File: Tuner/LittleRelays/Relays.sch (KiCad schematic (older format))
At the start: 86 parts, among them J1 Conn_01x03, J10 Conn_01x02, J11 Conn_01x02, J12 Conn_01x01, J13 Conn_01x01, J14 Conn_01x01, J15 Conn_01x01, J16 Conn_01x02, J17 Conn_02x10_Odd_Even, J18 Conn_01x02, J19 Conn_01x03, J2 Conn_01x03, J3 Conn_01x03, J4 Conn_01x03, J5 Conn_01x03, J6 Conn_01x03, J7 Conn_01x03, J8 Conn_01x02, J9 Conn_01x02

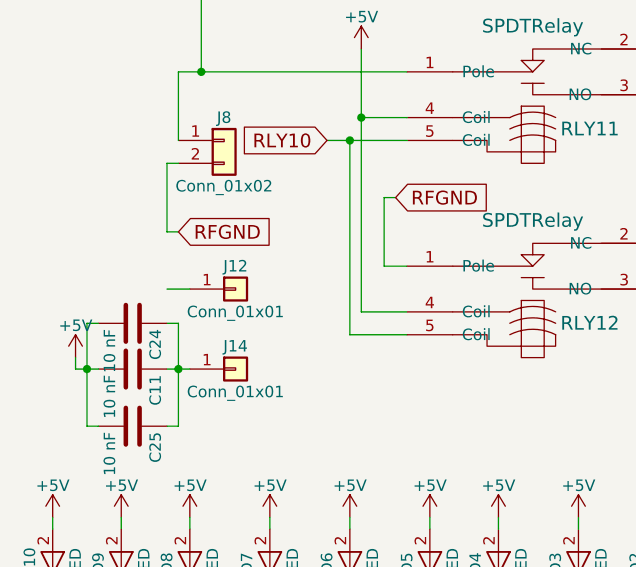
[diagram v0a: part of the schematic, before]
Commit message: Error in pinout HK19F fixed
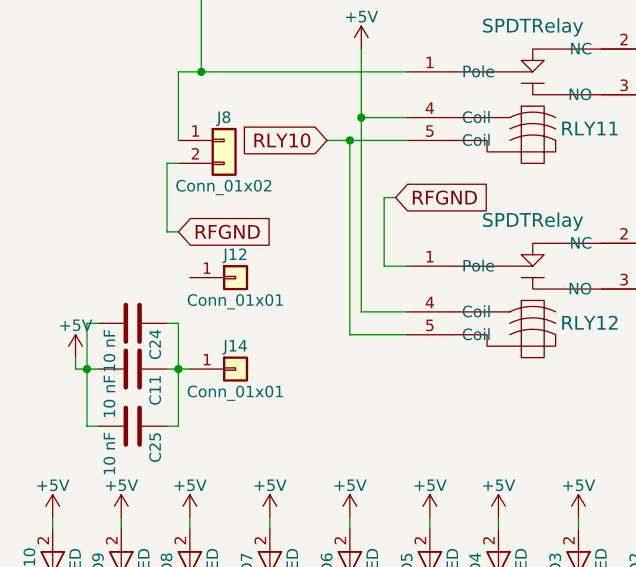
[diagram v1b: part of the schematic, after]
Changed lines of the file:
@@
 RLY10
-$Comp
-L Conn_01x01 J12
-U 1 1 5B1981D8
-P 1650 5400
-F 0 "J12" H 1650 5500 50  0000 C CNN
-F 1 "Conn_01x01" H 1650 5300 50  0000 C CNN
-F 2 "Connectors:1pin" H 1650 5400 50  0001 C CNN
-F 3 "" H 1650 5400 50  0001 C CNN
-	1    1650 5400
-	1    0    0    -1
-$EndComp
 $Comp
 L C C24
@@
 	7950 5400 8300 5400
 Wire Wire Line
-	1350 5400 1450 5400
-Wire Wire Line
 	1350 5550 1400 5550
 Wire Wire Line
 	1400 5550 1400 6000
 Connection ~ 1400 5750
-Wire Wire Line
-	1000 5550 1000 6000
 Wire Wire Line
 	1000 5550 1050 5550
@@
 	0    1    1    0
 $EndComp
+Wire Wire Line
+	1000 5550 1000 6000
+$Comp
+L Conn_01x01 J12
+U 1 1 5BCFCED9
+P 1650 5350
+F 0 "J12" H 1650 5450 50  0000 C CNN
+F 1 "Conn_01x01" H 1650 5250 50  0000 C CNN
+F 2 "Connectors:1pin" H 1650 5350 50  0001 C CNN
+F 3 "" H 1650 5350 50  0001 C CNN
+	1    1650 5350
+	1    0    0    -1
+$EndComp
 $EndSCHEMATC

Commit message: JLCPCB Nov 1 2018
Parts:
- removed C26: 10 nF, Capacitors_THT:C_Disc_D5.0mm_W2.5mm_P2.50mm, symbol C
- removed C27: 10 nF, Capacitors_THT:C_Disc_D5.0mm_W2.5mm_P5.00mm, symbol C
- added J20, J21, J22, J23, J24, J25, J26, J27, J28: Conn_01x01, tuner:SOLDERJUMPER, symbol Conn_01x01
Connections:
- net RFGND: now also J22.1 (Pin_1)
- net at J9.2 (Pin_2), RLY10.2 (NC): now also J23.1 (Pin_1)
- net at J10.2 (Pin_2), RLY10.3 (NO): now also J24.1 (Pin_1)
- net at J13.1 (Pin_1): now also J25.1 (Pin_1), J26.1 (Pin_1)
- net at J15.1 (Pin_1): now also J27.1 (Pin_1), J28.1 (Pin_1)
- net at J16.2 (Pin_2), RLY12.3 (NO): now also J21.1 (Pin_1)
- net at J11.2 (Pin_2), RLY12.2 (NC): now also J20.1 (Pin_1)
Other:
- moved on the sheet: J13, J15

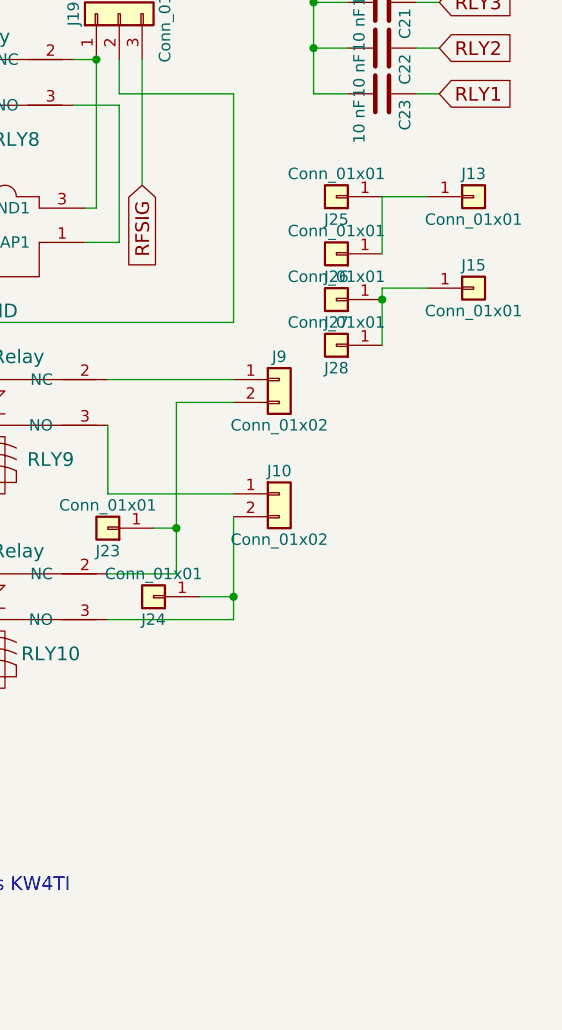
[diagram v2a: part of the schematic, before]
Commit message: Added extra capacitors between relay power and ground posts
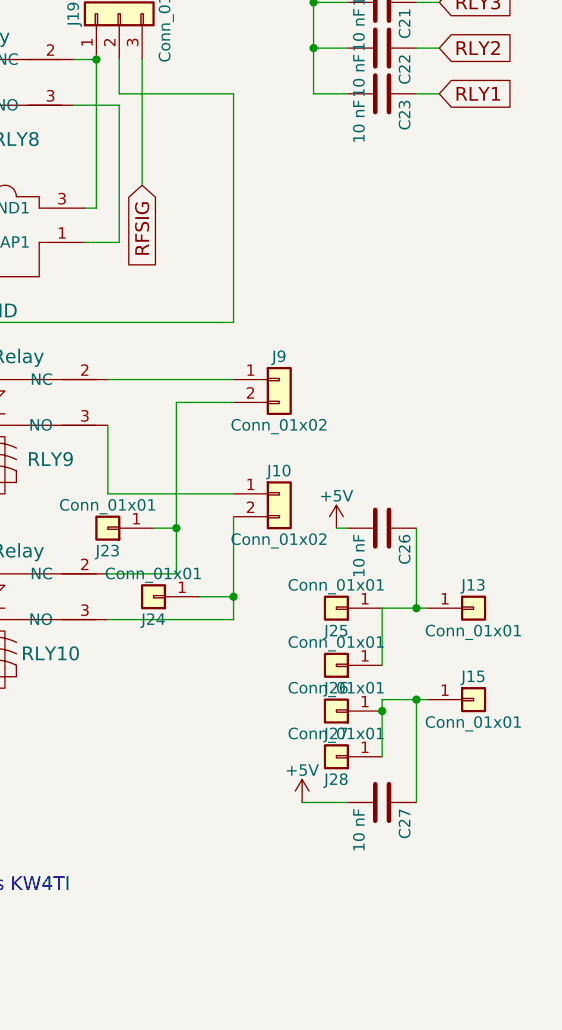
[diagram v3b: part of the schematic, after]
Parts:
- added C26, C27: 10 nF, Capacitors_THT:C_Disc_D5.0mm_W2.5mm_P2.50mm, symbol C
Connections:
- net +5V: now also C26.2, C27.2
- net at J13.1 (Pin_1), J25.1 (Pin_1), J26.1 (Pin_1): now also C26.1
- net at J15.1 (Pin_1), J27.1 (Pin_1), J28.1 (Pin_1): now also C27.1
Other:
- moved on the sheet: J13, J15, J25, J26, J27, J28
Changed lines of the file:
@@
 L Conn_01x01 J13
 U 1 1 5B19804D
-P 10950 3650
-F 0 "J13" H 10950 3750 50  0000 C CNN
-F 1 "Conn_01x01" H 10950 3550 50  0000 C CNN
-F 2 "Connectors:1pin" H 10950 3650 50  0001 C CNN
-F 3 "" H 10950 3650 50  0001 C CNN
-	1    10950 3650
+P 10950 5450
+F 0 "J13" H 10950 5550 50  0000 C CNN
+F 1 "Conn_01x01" H 10950 5350 50  0000 C CNN
+F 2 "Connectors:1pin" H 10950 5450 50  0001 C CNN
+F 3 "" H 10950 5450 50  0001 C CNN
+	1    10950 5450
 	1    0    0    -1
 $EndComp
@@
 L Conn_01x01 J15
 U 1 1 5B19812D
-P 10950 4050
-F 0 "J15" H 10950 4150 50  0000 C CNN
-F 1 "Conn_01x01" H 10950 3950 50  0000 C CNN
-F 2 "Connectors:1pin" H 10950 4050 50  0001 C CNN
-F 3 "" H 10950 4050 50  0001 C CNN
-	1    10950 4050
+P 10950 5850
+F 0 "J15" H 10950 5950 50  0000 C CNN
+F 1 "Conn_01x01" H 10950 5750 50  0000 C CNN
+F 2 "Connectors:1pin" H 10950 5850 50  0001 C CNN
+F 3 "" H 10950 5850 50  0001 C CNN
+	1    10950 5850
 	1    0    0    -1
 $EndComp
@@
 RLY9
 $Comp
-L +5V #PWR24
+L +5V #PWR25
 U 1 1 5BA3849B
 P 10250 1300
-F 0 "#PWR24" H 10250 1150 50  0001 C CNN
+F 0 "#PWR25" H 10250 1150 50  0001 C CNN
 F 1 "+5V" H 10250 1440 50  0000 C CNN
 F 2 "" H 10250 1300 50  0001 C CNN
@@
 L Conn_01x01 J25
 U 1 1 5BD818DE
-P 10350 3650
-F 0 "J25" H 10350 3750 50  0000 C CNN
-F 1 "Conn_01x01" H 10350 3550 50  0000 C CNN
-F 2 "tuner:SOLDERJUMPER" H 10350 3650 50  0001 C CNN
-F 3 "" H 10350 3650 50  0001 C CNN
-	1    10350 3650
+P 10350 5450
+F 0 "J25" H 10350 5550 50  0000 C CNN
+F 1 "Conn_01x01" H 10350 5350 50  0000 C CNN
+F 2 "tuner:SOLDERJUMPER" H 10350 5450 50  0001 C CNN
+F 3 "" H 10350 5450 50  0001 C CNN
+	1    10350 5450
 	-1   0    0    1
 $EndComp
@@
 L Conn_01x01 J26
 U 1 1 5BD81AB9
-P 10350 3900
-F 0 "J26" H 10350 4000 50  0000 C CNN
-F 1 "Conn_01x01" H 10350 3800 50  0000 C CNN
-F 2 "tuner:SOLDERJUMPER" H 10350 3900 50  0001 C CNN
-F 3 "" H 10350 3900 50  0001 C CNN
-	1    10350 3900
+P 10350 5700
+F 0 "J26" H 10350 5800 50  0000 C CNN
+F 1 "Conn_01x01" H 10350 5600 50  0000 C CNN
+F 2 "tuner:SOLDERJUMPER" H 10350 5700 50  0001 C CNN
+F 3 "" H 10350 5700 50  0001 C CNN
+	1    10350 5700
 	-1   0    0    1
 $EndComp
@@
 L Conn_01x01 J27
 U 1 1 5BD8205D
-P 10350 4100
-F 0 "J27" H 10350 4200 50  0000 C CNN
-F 1 "Conn_01x01" H 10350 4000 50  0000 C CNN
-F 2 "tuner:SOLDERJUMPER" H 10350 4100 50  0001 C CNN
-F 3 "" H 10350 4100 50  0001 C CNN
-	1    10350 4100
+P 10350 5900
+F 0 "J27" H 10350 6000 50  0000 C CNN
+F 1 "Conn_01x01" H 10350 5800 50  0000 C CNN
+F 2 "tuner:SOLDERJUMPER" H 10350 5900 50  0001 C CNN
+F 3 "" H 10350 5900 50  0001 C CNN
+	1    10350 5900
 	-1   0    0    1
 $EndComp
@@
 L Conn_01x01 J28
 U 1 1 5BD82344
-P 10350 4300
-F 0 "J28" H 10350 4400 50  0000 C CNN
-F 1 "Conn_01x01" H 10350 4200 50  0000 C CNN
-F 2 "tuner:SOLDERJUMPER" H 10350 4300 50  0001 C CNN
-F 3 "" H 10350 4300 50  0001 C CNN
-	1    10350 4300
+P 10350 6100
+F 0 "J28" H 10350 6200 50  0000 C CNN
+F 1 "Conn_01x01" H 10350 6000 50  0000 C CNN
+F 2 "tuner:SOLDERJUMPER" H 10350 6100 50  0001 C CNN
+F 3 "" H 10350 6100 50  0001 C CNN
+	1    10350 6100
 	-1   0    0    1
 $EndComp
@@
 	1000 5550 1000 6000
 Wire Wire Line
-	10550 3900 10550 3650
-Wire Wire Line
-	10550 3650 10750 3650
-Wire Wire Line
-	10550 4050 10550 4300
-Wire Wire Line
-	10550 4050 10750 4050
-Connection ~ 10550 4100
+	10550 5700 10550 5450
+Wire Wire Line
+	10550 5450 10750 5450
+Wire Wire Line
+	10550 5850 10550 6100
+Wire Wire Line
+	10550 5850 10750 5850
+Connection ~ 10550 5900
 Wire Wire Line
 	9550 5100 9650 5100
@@
 	3600 5050 3750 5050
 Connection ~ 3750 5050
+$Comp
+L +5V #PWR26
+U 1 1 5DDB9BB3
+P 10350 5100
+F 0 "#PWR26" H 10350 4950 50  0001 C CNN
+F 1 "+5V" H 10350 5240 50  0000 C CNN
+F 2 "" H 10350 5100 50  0001 C CNN
+F 3 "" H 10350 5100 50  0001 C CNN
+	1    10350 5100
+	1    0    0    -1
+$EndComp
+$Comp
+L C C26
+U 1 1 5DDBA4A3
+P 10550 5100
+F 0 "C26" H 10575 5200 50  0000 L CNN
+F 1 "10 nF" H 10575 5000 50  0000 L CNN
+F 2 "Capacitors_THT:C_Disc_D5.0mm_W2.5mm_P2.50mm" H 10588 4950 50  0001 C CNN
+F 3 "" H 10550 5100 50  0001 C CNN
+	1    10550 5100
+	0    1    1    0
+$EndComp
+Wire Wire Line
+	10400 5100 10350 5100
+Wire Wire Line
+	10700 5100 10700 5450
+Connection ~ 10700 5450
+$Comp
+L +5V #PWR24
+U 1 1 5DDBACE8
+P 10200 6300
+F 0 "#PWR24" H 10200 6150 50  0001 C CNN
+F 1 "+5V" H 10200 6440 50  0000 C CNN
+F 2 "" H 10200 6300 50  0001 C CNN
+F 3 "" H 10200 6300 50  0001 C CNN
+	1    10200 6300
+	1    0    0    -1
+$EndComp
+$Comp
+L C C27
+U 1 1 5DDBAE6B
+P 10550 6300
+F 0 "C27" H 10575 6400 50  0000 L CNN
+F 1 "10 nF" H 10575 6200 50  0000 L CNN
+F 2 "Capacitors_THT:C_Disc_D5.0mm_W2.5mm_P2.50mm" H 10588 6150 50  0001 C CNN
+F 3 "" H 10550 6300 50  0001 C CNN
+	1    10550 6300
+	0    1    1    0
+$EndComp
+Wire Wire Line
+	10700 5850 10700 6300
+Connection ~ 10700 5850
+Wire Wire Line
+	10400 6300 10200 6300
 $EndSCHEMATC

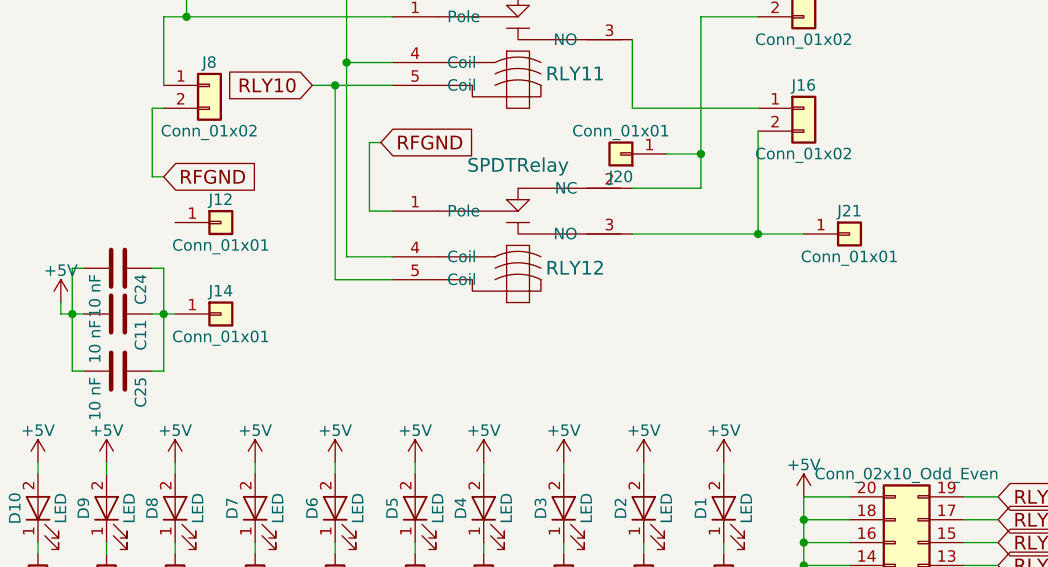
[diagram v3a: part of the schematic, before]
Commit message: Added extra capacitors to ground to large relay boards
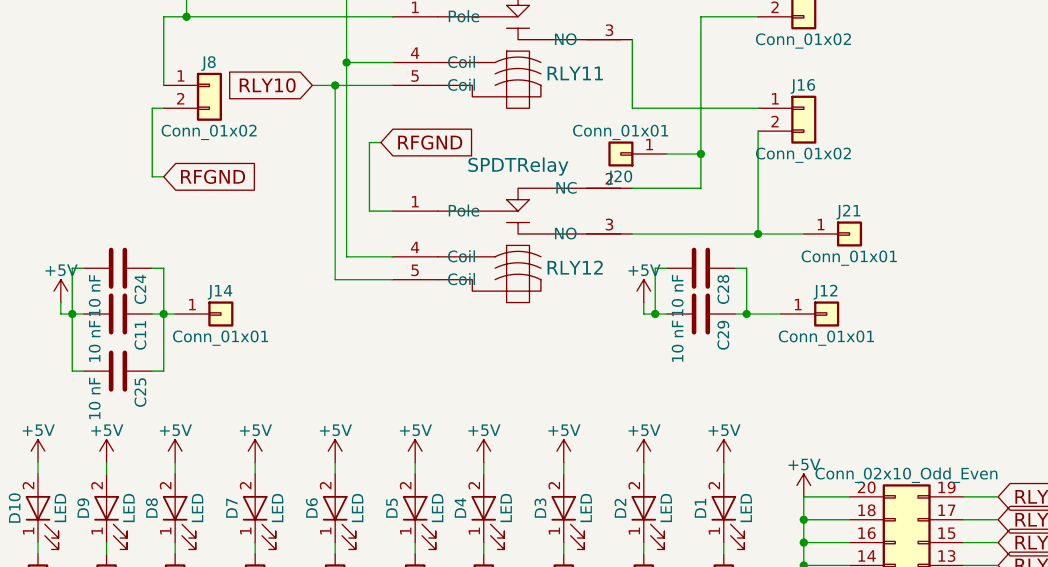
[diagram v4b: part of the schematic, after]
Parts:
- added C28, C29: 10 nF, Capacitors_THT:C_Disc_D5.0mm_W2.5mm_P5.00mm, symbol C
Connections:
- net +5V: now also C28.2, C29.2
- net at J12.1 (Pin_1): now also C28.1, C29.1
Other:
- moved on the sheet: J12
